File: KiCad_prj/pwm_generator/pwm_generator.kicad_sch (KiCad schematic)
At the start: 18 parts, among them J1 MLW20A, J2 MLW10A, U1 LM2664 / LM2665, U2 74HC14, U3 TL431DBV

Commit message: Pocatek prace na DPS
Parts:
- removed JP1: DC, Jumper:SolderJumper-2_P1.3mm_Open_RoundedPad1.0x1.5mm, symbol Jumper:SolderJumper_2_Open
- removed JP2: AC, Jumper:SolderJumper-2_P1.3mm_Open_RoundedPad1.0x1.5mm, symbol Jumper:SolderJumper_2_Open
- removed U3: TL431DBV, Package_TO_SOT_SMD:SOT-23-5, symbol Reference_Voltage:TL431DBV
- added C28: 100p, Capacitor_SMD:C_0805_2012Metric, symbol Device:C
- added C5: 100n, Capacitor_SMD:C_0805_2012Metric, symbol Device:C
- added R38, R39: 22R, Resistor_SMD:R_0805_2012Metric, symbol Device:R
- added R40: 100R, Resistor_SMD:R_0805_2012Metric, symbol Device:R
- added U3: TL431DBZ, Package_TO_SOT_SMD:SOT-23, symbol Reference_Voltage:TL431DBZ
- renumbered R5 to R4, R4 to R5, R7 to R6, R6 to R7
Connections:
- net Triangle Wave Generator/SAMPLING is gone; now on net PWM_CHA: U2.5
- net +5V: now also J1.1 (Pin_1); no longer J1.14 (Pin_14), J1.2 (Pin_2), J1.8 (Pin_8), J2.4 (Pin_4)
- net CHA: now also J1.14 (Pin_14), R4.1; no longer J1.10 (Pin_10), R5.1
- net CHB: now also J1.10 (Pin_10), R6.1; no longer J1.16 (Pin_16), R7.1
- net GND: now also J1.2 (Pin_2), C28.2, C5.1, U3.3 (A); no longer J1.1 (Pin_1)
- net PWM_CHA: no longer U2.1
- net SAMP: now also J1.18 (Pin_18); no longer J1.4 (Pin_4)
- net U_{REF}: now also J2.4 (Pin_4), C5.2, U3.1 (K), U3.2 (REF)
- net Wave Shaper/ACDC: now also J2.2 (Pin_2); no longer J2.6 (Pin_6)
- net Wave Shaper/INPUT_SIGNAL: now also J2.6 (Pin_6); no longer J2.2 (Pin_2)
- net at R7.2: now also U2.11, U2.12; no longer U2.10
- net at U2.8: now also R4.2; no longer R2.2
- net at U2.6, U2.9: now also R5.2; no longer R3.2
- net at U2.2, U2.3: now also R2.2; no longer R4.2
- net at U2.4: now also R3.2; no longer R5.2
- net CHAINV renamed ~{CHA}
- net ~{CHA}: now also R5.1; no longer R4.1
- removed net CHBINV: J1.18 (Pin_18), R6.1
- net SAMPINV renamed TWG_OUT
- net TWG_OUT: now also R39.1; no longer R3.1
- new net: R6.2, U2.10
- new net: C28.1, R40.2
- new net TRIANGLE_IN: R38.2
- new net TRIANGLE_OUT: R39.2
- new net TWG_IN: J1.4 (Pin_4), R38.1, R40.1
- new net Triangle Wave Generator/~{SAMPLING}: U2.1
- new net ~{CHB}: J1.8 (Pin_8), R7.1
- new net ~{SAMP}: J1.16 (Pin_16), R3.1
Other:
- sheet Triangle Wave Generator ports: added ~{SAMPLING}; removed SAMPLING
- sheet Wave Shaper ports: added ~{SIGNAL_REF}; removed SIGNAL_REF_INV
- moved on the sheet: C1, C2, C3, C4, J1, J2, R1, R2, R3, R4, R5, R6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

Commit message: Dokoncene trasy na DPS pwm_generator
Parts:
- added C29, C32, C33: 100n, Capacitor_SMD:C_0805_2012Metric, symbol Device:C
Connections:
- net +5V: now also C29.2, C32.2, C33.2
- net GND: now also C29.1, C32.1, C33.1
- net U_{REF}: now also J2.2 (Pin_2); no longer J2.4 (Pin_4)
- net Wave Shaper/ACDC: now also J2.4 (Pin_4); no longer J2.2 (Pin_2)
- net Wave Shaper/COMPENSATION_NEG: now also J2.8 (Pin_8); no longer J2.10 (Pin_10)
- net Wave Shaper/COMPENSATION_POS: now also J2.6 (Pin_6); no longer J2.8 (Pin_8)
- net Wave Shaper/INPUT_SIGNAL: now also J2.10 (Pin_10); no longer J2.6 (Pin_6)

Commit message: precislovani
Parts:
- renumbered C2 to C1, C3 to C2, C4 to C3, C29 to C4, C1 to C6, C28 to C7, C32 to C8, C33 to C9, J2 to J1, J1 to J2, R40 to R10, R39 to R8, R38 to R9, U3 to U2, U2 to U3

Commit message: Uprava DPS generatoru - popisky
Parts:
- added D7: LED, LED_SMD:LED_0805_2012Metric, symbol Device:LED
- added R41: 560R, Resistor_SMD:R_0805_2012Metric, symbol Device:R
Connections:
- net +5V: now also R41.2
- net GND: now also D7.1 (K)
- net SAMP renamed TRIG
- net Triangle Wave Generator/~{SAMPLING} renamed Triangle Wave Generator/~{TRIGGER}
- net ~{SAMP} renamed ~{TRIG}
- new net: D7.2 (A), R41.1
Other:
- sheet Triangle Wave Generator ports: added ~{TRIGGER}; removed ~{SAMPLING}

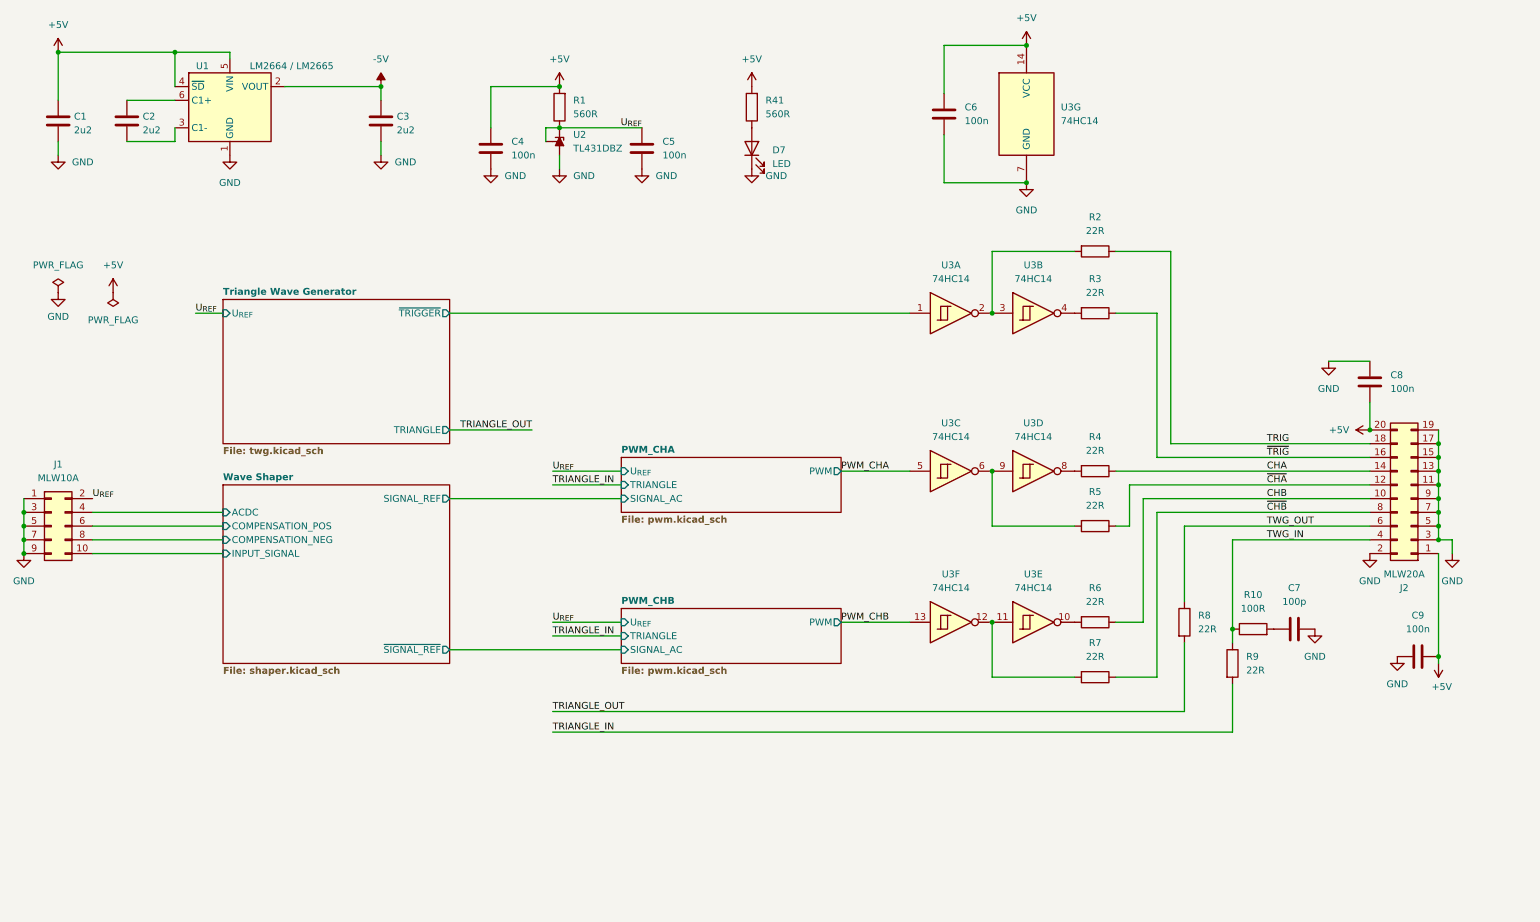
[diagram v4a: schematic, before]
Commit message: Pridany testpointy a jlcpcb bom reference
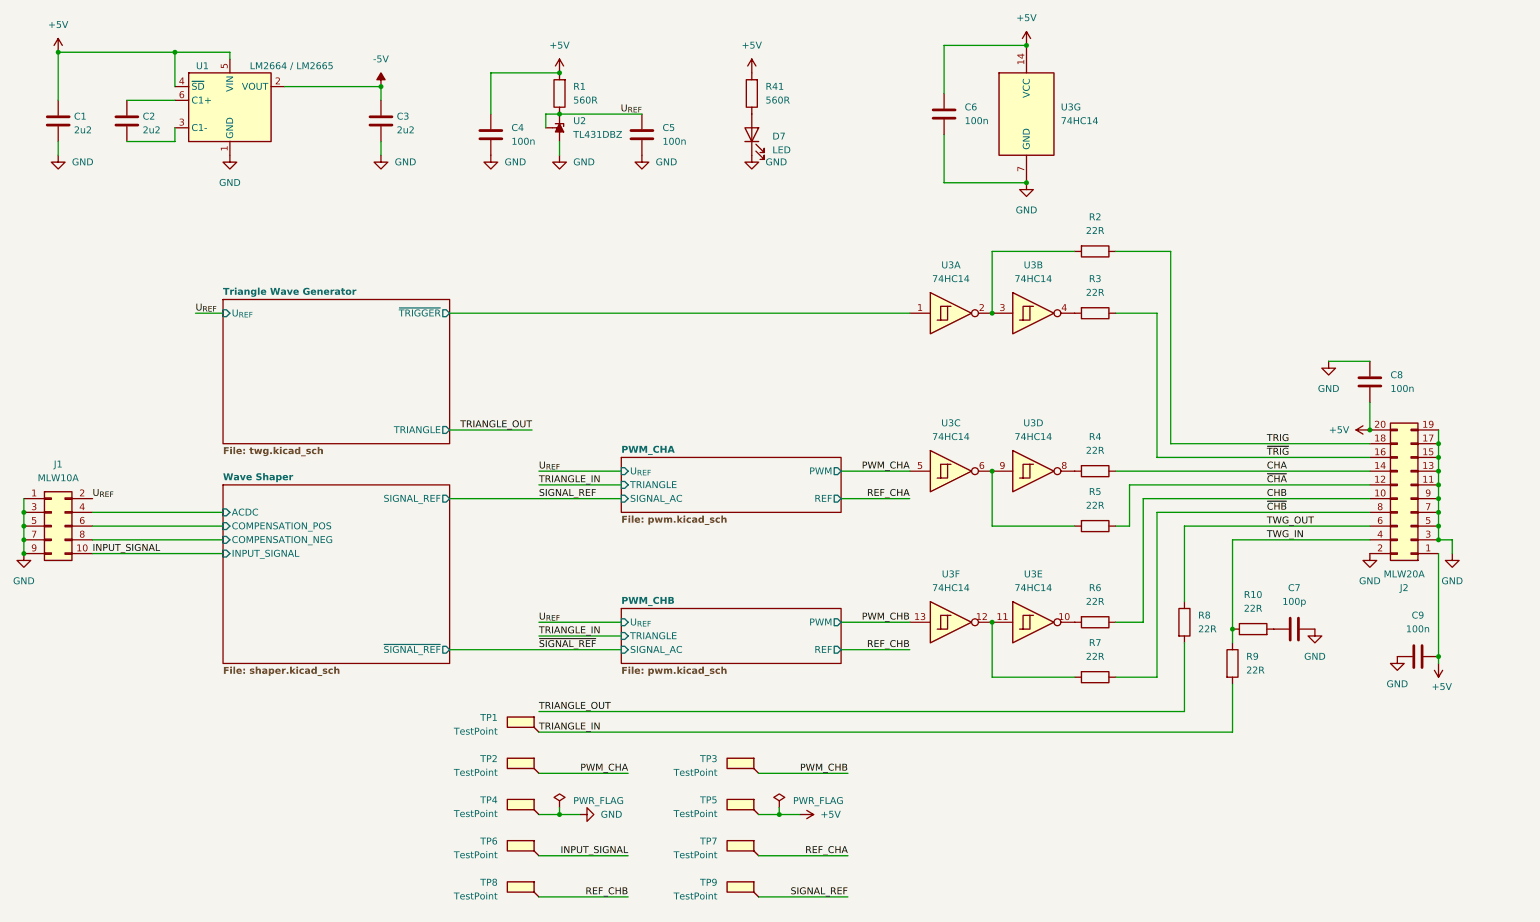
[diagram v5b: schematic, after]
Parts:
- added TP1, TP2, TP3, TP4, TP5, TP6, TP7, TP8, TP9: TestPoint, TestPoint:TestPoint_Loop_D1.80mm_Drill1.0mm_Beaded, symbol Connector:TestPoint_Flag
- C1, C2, C3: JLCPCB Part # C380334 -> C377773
- C4, C5, C6, C8, C9: JLCPCB Part # (none) -> C49678
- C7: JLCPCB Part # (none) -> C1790
- D7: JLCPCB Part # (none) -> C84256
- J1, J2: now left out of the parts list
- R1, R41: JLCPCB Part # (none) -> C28636
- R10: value 100R -> 22R; JLCPCB Part # (none) -> C17561
- R2, R3, R4, R5, R6, R7, R8, R9: JLCPCB Part # (none) -> C17561
- U2: JLCPCB Part # (none) -> C181103
- U3: JLCPCB Part # (none) -> C5605
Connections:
- net +5V: now also TP5.1
- net GND: now also TP4.1
- net PWM_CHA: now also TP2.1
- net PWM_CHB: now also TP3.1
- net TRIANGLE_IN: now also TP1.1
- net Wave Shaper/INPUT_SIGNAL renamed INPUT_SIGNAL
- net INPUT_SIGNAL: now also TP6.1
- new net REF_CHA: TP7.1
- new net REF_CHB: TP8.1
- new net SIGNAL_REF: TP9.1
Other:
- sheet PWM_CHA ports: added REF; removed none
- sheet PWM_CHB ports: added REF; removed none
- moved on the sheet: C4, C5, D7, R1, R41, U2

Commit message: Doplnene testovaci body a popisky
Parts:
- added TP11: U_{REF}, TestPoint:TestPoint_Loop_D1.80mm_Drill1.0mm_Beaded, symbol Connector:TestPoint_Flag
- added TP4: Trigger, TestPoint:TestPoint_Loop_D1.80mm_Drill1.0mm_Beaded, symbol Connector:TestPoint_Flag
- TP1: value TestPoint -> Triangle In
- TP10: renamed from TP8; value TestPoint -> Ref ChB
- TP2: value TestPoint -> PWM ChA
- TP3: value TestPoint -> PWM ChB
- TP5: value TestPoint -> SUP +5V
- TP6: renamed from TP4; value TestPoint -> SUP GND
- TP7: renamed from TP6; value TestPoint -> Signal In
- TP8: renamed from TP9; value TestPoint -> Signal Ref
- TP9: renamed from TP7; value TestPoint -> Ref ChA
- renumbered D7 to D1, R9 to R10, R10 to R11, R41 to R2, R2 to R3, R3 to R4, R4 to R5, R5 to R6, R6 to R7, R7 to R8, R8 to R9
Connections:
- net U_{REF}: now also TP11.1
- net TRIGGER: now reaches R3.2, U3.2, U3.3
- net TRIGGER: now also TP4.1
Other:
- moved on the sheet: TP10, TP2, TP3, TP5, TP6, TP7, TP8, TP9

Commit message: pwm_generator 1.0 odeslan do vyroby
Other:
- note added: "Pro diferenciální linku dle AM26LS32 - zakončení 120 ohm (118 ohm výstup) - NEXT dělič napětí 5 V na 1,7 V, pro FEXT 0,85 V - sestava (22 zde):150:(180 výstup):150:(22 zde) - zatížení výstupu 12 mA"
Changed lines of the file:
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@@
 		(rev "${REVISION}")
+	)
+	(text "Pro diferenciální linku dle AM26LS32\n- zakončení 120 ohm (118 ohm výstup)\n- NEXT dělič napětí 5 V na 1,7 V, pro FEXT 0,85 V\n- sestava (22 zde):150:(180 výstup):150:(22 zde)\n- zatížení výstupu 12 mA"
+		(exclude_from_sim no)
+		(at 232.664 84.328 0)
+		(effects
+			(font
+				(size 1.27 1.27)
+			)
+			(justify left)
+		)
 	)
 	(junction
